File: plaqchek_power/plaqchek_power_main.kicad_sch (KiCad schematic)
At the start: 28 parts, among them U10 LM34601, U12 TPS54202DDC, U15 TPS62175DQC

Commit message: finish schematic
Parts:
- removed U10: LM34601, symbol plaqchek_mlb:LM34601
- added R10, R19, R20, R21, R22, R23, R24, R25, R29, R30: 0R, symbol Device:R_Small_US
- added TP1, TP2, TP3, TP4, TP5, TP6: TestPoint, symbol Connector:TestPoint
- added U2: LM34601, symbol plaqchek:LM34601
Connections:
- net +12V: now also R20.2, R21.2, R22.2; no longer C19.1, C23.1, C24.1, C25.1, C32.1, C39.2, U12.3 (VIN), U15.2 (VIN), U15.3 (EN)
- net +3V3: now also R25.1, TP6.1; no longer C34.1, C35.1, L2.2, R22.1
- net +6V: now also R19.2, R24.1, TP2.1; no longer C40.2, L3.2, R26.1, U15.10 (VOS), U15.8 (~{SLEEP})
- net -6V5: now also R23.1, TP4.1; no longer C23.2, C24.2, C25.2, C27.1, C29.2, C30.2, R24.1
- net GND: now also U2.5 (BIAS)
- net at R23.1, R24.2: now also U2.9 (FB)
- net at U12.5 (EN): now also R10.1
- net at C28.1: now also U2.3 (CBOOT)
- net at C28.2, L1.1: now also U2.1 (SW), U2.2 (SW)
- net at R21.2: now also U2.8 (PGOOD)
- net at C27.2: now also U2.4 (VCC)
- new net: C23.1, C24.1, C25.1, R20.1, R29.2, U2.13 (VIN), U2.14 (VIN)
- new net: C23.2, C24.2, C25.2, C27.1, C29.2, C30.2, R23.2, R24.1, TP3.1, U2.10 (AGND), U2.15 (PGND), U2.16 (PGND)
- new net: C34.1, C35.1, L2.2, R22.1, R25.2, TP5.1
- new net: C19.1, C32.1, R22.1, U12.3 (VIN)
- new net: R19.1, U15.8 (~{SLEEP})
- new net: C39.2, R21.1, R30.1, U15.2 (VIN)
- new net: C40.2, L3.2, R24.2, R26.1, TP1.1, U15.10 (VOS)
- new net: R29.1, U2.12 (EN)
- new net: R30.2, U15.3 (EN)
- no-connect marks 4 -> 5
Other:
- moved on the sheet: C19, C23, C24, C25, C27, C28, C29, C30, C32, C33, C34, C35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

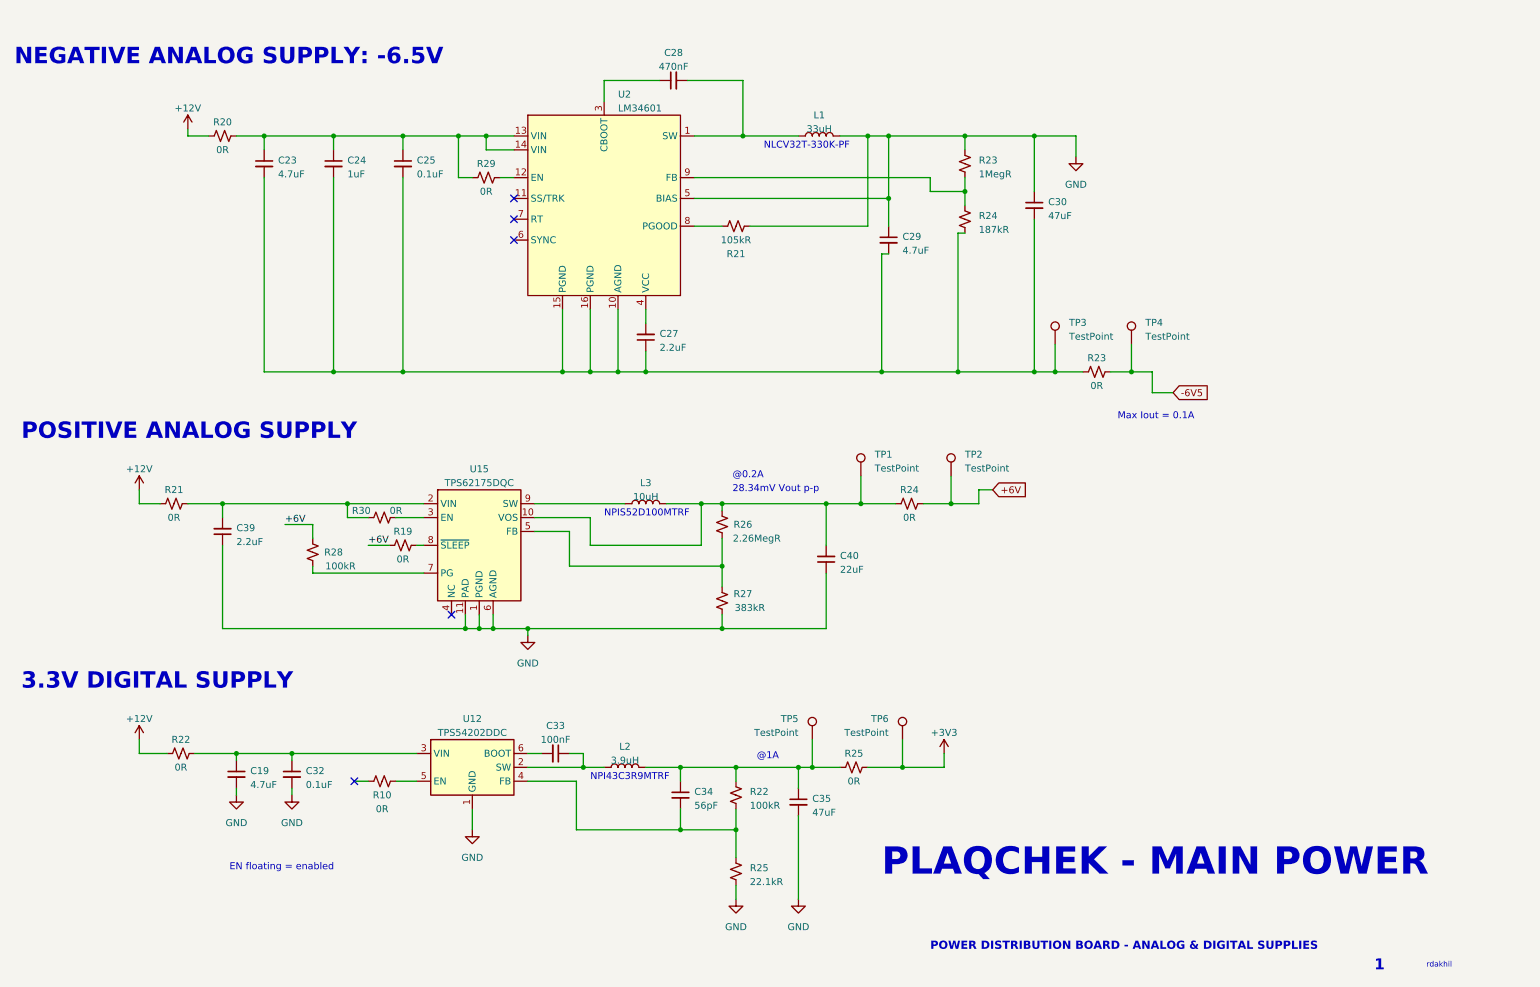
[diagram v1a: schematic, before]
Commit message: more footprints and some value fixes
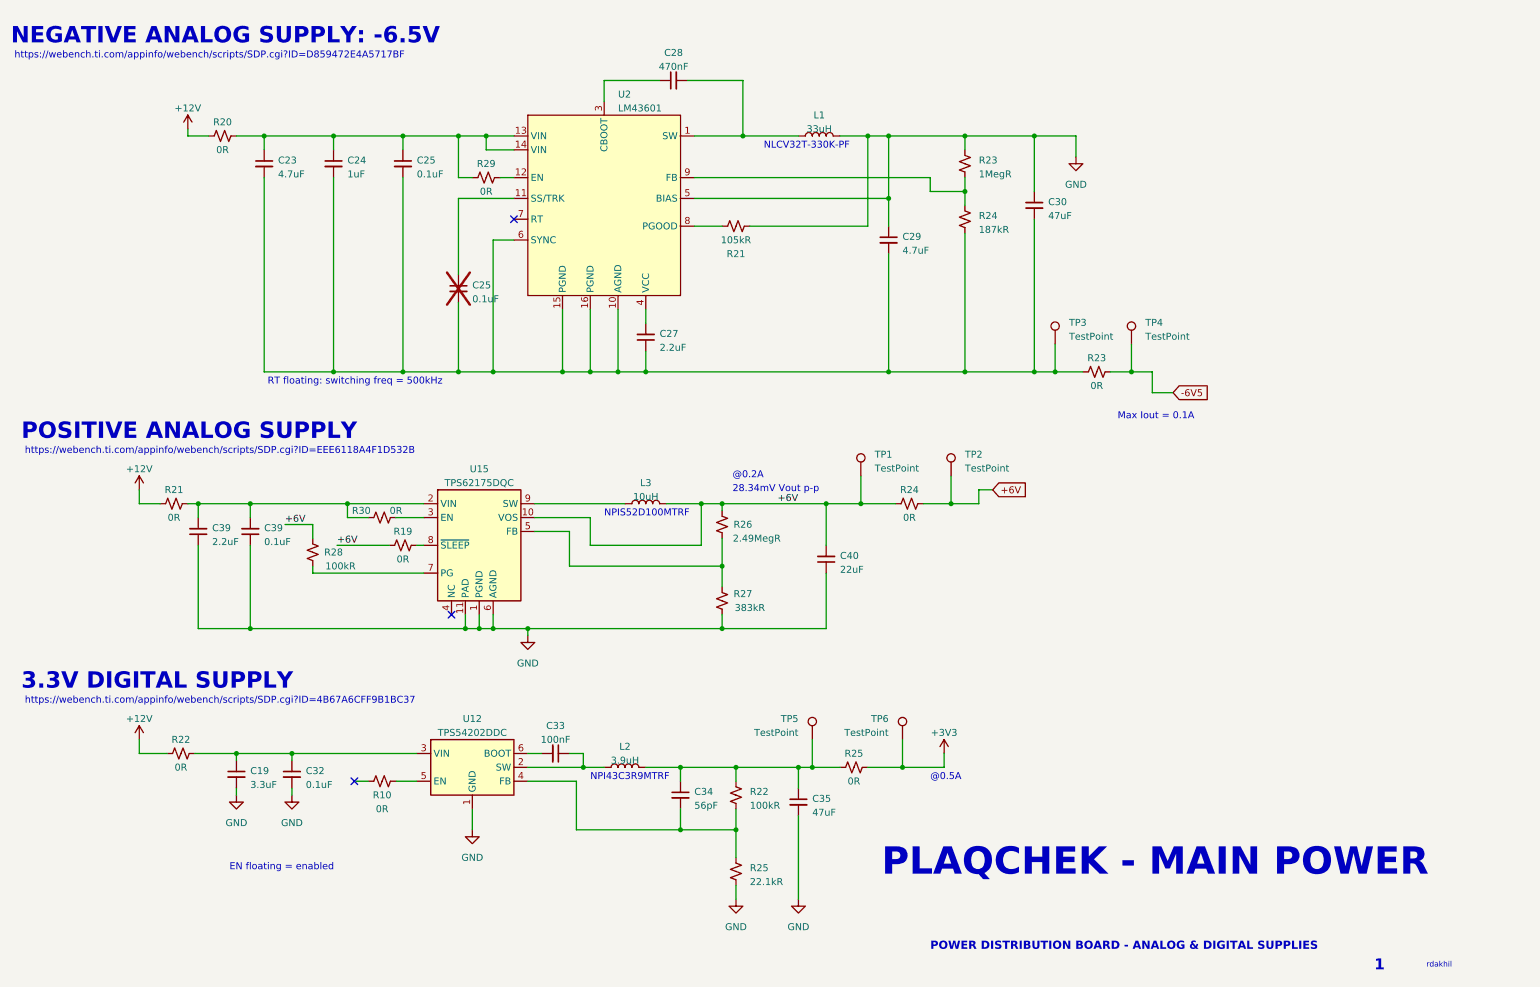
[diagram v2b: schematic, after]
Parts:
- added C25, C39: 0.1uF, Capacitor_SMD:C_0603_1608Metric_Pad1.08x0.95mm_HandSolder, symbol Device:C_Small
- C19: value 4.7uF -> 3.3uF; footprint (none) -> Capacitor_SMD:C_0603_1608Metric_Pad1.08x0.95mm_HandSolder
- C23, C29, C40: footprint (none) -> Capacitor_SMD:C_0805_2012Metric_Pad1.18x1.45mm_HandSolder
- C24, C25, C27, C28, C32, C33, C34, C39: footprint (none) -> Capacitor_SMD:C_0603_1608Metric_Pad1.08x0.95mm_HandSolder
- C30, C35: footprint (none) -> Capacitor_SMD:C_1206_3216Metric_Pad1.33x1.80mm_HandSolder
- R26: value 2.26MegR -> 2.49MegR
- U2: value LM34601 -> LM43601
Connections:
- net +6V: now also C40.2, L3.2, R24.2, R26.1, TP1.1, U15.10 (VOS)
- net GND: now also C39.1
- net at C23.2, C24.2, C25.2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: now also U2.6 (SYNC), C25.2
- net at C39.2, R21.1, R30.1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: now also C39.2
- net at U2.11 (SS/TRK): now also C25.1
- no-connect marks 5 -> 3
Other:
- note added: "@0.5A"
- note added: "RT floating: switching freq = 500kHz"
- note added: "https://webench.ti.com/appinfo/webench/scripts/SDP.cgi?ID=4B67A6CFF9B1BC37"
- note added: "https://webench.ti.com/appinfo/webench/scripts/SDP.cgi?ID=D859472E4A5717BF"
- note added: "https://webench.ti.com/appinfo/webench/scripts/SDP.cgi?ID=EEE6118A4F1D532B"
- note removed: "@1A"
- moved on the sheet: C39

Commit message: finish main logic board PCB routing
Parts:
- L1: footprint (none) -> Inductor_SMD:L_1210_3225Metric_Pad1.42x2.65mm_HandSolder
- R10, R19, R20, R21, R22, R23, R24, R25, R26, R27, R28, R29, R30: footprint (none) -> Resistor_SMD:R_0603_1608Metric_Pad0.98x0.95mm_HandSolder
- U2: footprint (none) -> Package_SO:HTSSOP-16-1EP_4.4x5mm_P0.65mm_EP3.4x5mm
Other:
- note added: "744025100"
- note added: "78438336100"
- note added: "LM43601PWPR"
- note removed: "NPI43C3R9MTRF"
- note removed: "NPIS52D100MTRF"
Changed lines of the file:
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@@
     (effects (font (size 1 1)) (justify left bottom))
+  )
+  (text "LM43601PWPR" (at 109.22 35.56 0)
+    (effects (font (size 1.27 1.27)) (justify left bottom))
   )
   (text "NLCV32T-330K-PF" (at 156.21 43.18 0)
     (effects (font (size 1.27 1.27)) (justify left bottom))
   )
-  (text "NPI43C3R9MTRF\n" (at 124.46 158.75 0)
+  (text "744025100\n" (at 124.46 158.75 0)
     (effects (font (size 1.27 1.27)) (justify left bottom))
   )
@@
     (effects (font (size 1.27 1.27)) (justify left bottom))
   )
-  (text "NPIS52D100MTRF" (at 127 110.49 0)
+  (text "78438336100\n" (at 127 110.49 0)
     (effects (font (size 1.27 1.27)) (justify left bottom))
   )
@@
       (effects (font (size 1.27 1.27)))
     )
-    (property "Footprint" "" (at 57.15 40.64 0)
+    (property "Footprint" "Resistor_SMD:R_0603_1608Metric_Pad0.98x0.95mm_HandSolder" (at 57.15 40.64 0)
       (effects (font (size 1.27 1.27)) hide)
     )
@@
       (effects (font (size 1.27 1.27)) (justify left))
     )
-    (property "Footprint" "" (at 151.13 161.29 0)
+    (property "Footprint" "Resistor_SMD:R_0603_1608Metric_Pad0.98x0.95mm_HandSolder" (at 151.13 161.29 0)
       (effects (font (size 1.27 1.27)) hide)
     )
@@
       (effects (font (size 1.27 1.27)) (justify right))
     )
-    (property "Footprint" "" (at 193.04 45.72 0)
+    (property "Footprint" "Resistor_SMD:R_0603_1608Metric_Pad0.98x0.95mm_HandSolder" (at 193.04 45.72 0)
       (effects (font (size 1.27 1.27)) hide)
     )
@@
       (effects (font (size 1.27 1.27)))
     )
-    (property "Footprint" "" (at 90.17 115.57 0)
+    (property "Footprint" "Resistor_SMD:R_0603_1608Metric_Pad0.98x0.95mm_HandSolder" (at 90.17 115.57 0)
       (effects (font (size 1.27 1.27)) hide)
     )
@@
       (effects (font (size 1.27 1.27)))
     )
-    (property "Footprint" "" (at 48.26 107.95 0)
+    (property "Footprint" "Resistor_SMD:R_0603_1608Metric_Pad0.98x0.95mm_HandSolder" (at 48.26 107.95 0)
       (effects (font (size 1.27 1.27)) hide)
     )
@@
       (effects (font (size 1.27 1.27)))
     )
-    (property "Footprint" "" (at 151.13 57.15 0)
+    (property "Footprint" "Resistor_SMD:R_0603_1608Metric_Pad0.98x0.95mm_HandSolder" (at 151.13 57.15 0)
       (effects (font (size 1.27 1.27)) hide)
     )
@@
       (effects (font (size 1.27 1.27)) (justify left))
     )
-    (property "Footprint" "" (at 138.43 25.4 0)
+    (property "Footprint" "Package_SO:HTSSOP-16-1EP_4.4x5mm_P0.65mm_EP3.4x5mm" (at 138.43 25.4 0)
       (effects (font (size 1.27 1.27)) hide)
     )
@@
       (effects (font (size 1.27 1.27)) (justify left))
     )
-    (property "Footprint" "" (at 151.13 175.26 0)
+    (property "Footprint" "Resistor_SMD:R_0603_1608Metric_Pad0.98x0.95mm_HandSolder" (at 151.13 175.26 0)
       (effects (font (size 1.27 1.27)) hide)
     )
@@
       (effects (font (size 1.27 1.27)))
     )
-    (property "Footprint" "" (at 172.72 156.21 0)
+    (property "Footprint" "Resistor_SMD:R_0603_1608Metric_Pad0.98x0.95mm_HandSolder" (at 172.72 156.21 0)
       (effects (font (size 1.27 1.27)) hide)
     )
@@
       (effects (font (size 1.27 1.27)))
     )
-    (property "Footprint" "" (at 182.88 107.95 0)
+    (property "Footprint" "Resistor_SMD:R_0603_1608Metric_Pad0.98x0.95mm_HandSolder" (at 182.88 107.95 0)
       (effects (font (size 1.27 1.27)) hide)
     )
@@
       (effects (font (size 1.27 1.27)))
     )
-    (property "Footprint" "" (at 148.59 125.73 0)
+    (property "Footprint" "Resistor_SMD:R_0603_1608Metric_Pad0.98x0.95mm_HandSolder" (at 148.59 125.73 0)
       (effects (font (size 1.27 1.27)) hide)
     )
@@
       (effects (font (size 1.27 1.27)))
     )
-    (property "Footprint" "" (at 49.53 153.67 0)
+    (property "Footprint" "Resistor_SMD:R_0603_1608Metric_Pad0.98x0.95mm_HandSolder" (at 49.53 153.67 0)
       (effects (font (size 1.27 1.27)) hide)
     )
@@
       (effects (font (size 1.27 1.27)))
     )
-    (property "Footprint" "" (at 105.41 48.26 0)
+    (property "Footprint" "Resistor_SMD:R_0603_1608Metric_Pad0.98x0.95mm_HandSolder" (at 105.41 48.26 0)
       (effects (font (size 1.27 1.27)) hide)
     )
@@
       (effects (font (size 1.27 1.27)))
     )
-    (property "Footprint" "" (at 86.36 158.75 0)
+    (property "Footprint" "Resistor_SMD:R_0603_1608Metric_Pad0.98x0.95mm_HandSolder" (at 86.36 158.75 0)
       (effects (font (size 1.27 1.27)) hide)
     )
@@
       (effects (font (size 1.27 1.27)))
     )
-    (property "Footprint" "" (at 217.17 83.82 0)
+    (property "Footprint" "Resistor_SMD:R_0603_1608Metric_Pad0.98x0.95mm_HandSolder" (at 217.17 83.82 0)
       (effects (font (size 1.27 1.27)) hide)
     )
@@
       (effects (font (size 1.27 1.27)))
     )
-    (property "Footprint" "" (at 148.59 111.76 0)
+    (property "Footprint" "Resistor_SMD:R_0603_1608Metric_Pad0.98x0.95mm_HandSolder" (at 148.59 111.76 0)
       (effects (font (size 1.27 1.27)) hide)
     )
@@
       (effects (font (size 1.27 1.27)))
     )
-    (property "Footprint" "" (at 73.66 116.84 0)
+    (property "Footprint" "Resistor_SMD:R_0603_1608Metric_Pad0.98x0.95mm_HandSolder" (at 73.66 116.84 0)
       (effects (font (size 1.27 1.27)) hide)
     )
@@
       (effects (font (size 1.27 1.27)) (justify right))
     )
-    (property "Footprint" "" (at 193.04 55.88 0)
+    (property "Footprint" "Resistor_SMD:R_0603_1608Metric_Pad0.98x0.95mm_HandSolder" (at 193.04 55.88 0)
       (effects (font (size 1.27 1.27)) hide)
     )
@@
       (effects (font (size 1.27 1.27)))
     )
-    (property "Footprint" "" (at 86.36 110.49 0)
+    (property "Footprint" "Resistor_SMD:R_0603_1608Metric_Pad0.98x0.95mm_HandSolder" (at 86.36 110.49 0)
       (effects (font (size 1.27 1.27)) hide)
     )
@@
       (effects (font (size 1.27 1.27)))
     )
-    (property "Footprint" "" (at 166.37 40.64 0)
+    (property "Footprint" "Inductor_SMD:L_1210_3225Metric_Pad1.42x2.65mm_HandSolder" (at 166.37 40.64 0)
       (effects (font (size 1.27 1.27)) hide)
     )
@@
       (effects (font (size 1.27 1.27)) hide)
     )
-    (property "Datasheet" "~" (at 130.81 156.21 0)
-      (effects (font (size 1.27 1.27)) hide)
-    )
+    (property "Datasheet" "https://www.we-online.com/components/products/datasheet/744025100.pdf" (at 130.81 156.21 0)
+      (effects (font (size 1.27 1.27)) hide)
+    )

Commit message: finish power board routing, sensing board routing
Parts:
- removed C25: 0.1uF, Capacitor_SMD:C_0603_1608Metric_Pad1.08x0.95mm_HandSolder, symbol Device:C_Small
- removed R29: 0R, Resistor_SMD:R_0603_1608Metric_Pad0.98x0.95mm_HandSolder, symbol Device:R_Small_US
- added C40: 22uF, Capacitor_SMD:C_0805_2012Metric_Pad1.18x1.45mm_HandSolder, symbol Device:C_Small
- L2: value 3.9uH -> 10uH; footprint (none) -> plaqchek:744025100
- L3: footprint (none) -> plaqchek:78438336100
- TP1, TP2, TP3, TP4, TP5, TP6: footprint (none) -> TestPoint:TestPoint_Pad_D1.0mm
- U15: footprint Package_SON:WSON-10-1EP_2x3mm_P0.5mm_EP0.84x2.4mm_ThermalVias -> Package_SON:WSON-10-1EP_2x3mm_P0.5mm_EP0.84x2.4mm
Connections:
- net +6V: no longer C40.2, L3.2, R24.2, R26.1, TP1.1, U15.10 (VOS)
- net GND: now also U15.4 (NC), C40.1
- net VIN_-6V5: now reaches C23.1, C24.1, C25.1, R20.1, U2.13 (VIN), U2.14 (VIN)
- net VIN_-6V5: now also U2.12 (EN)
- net VOUT_-6V5: now reaches C23.2, C24.2, C25.2, C27.1, C29.2, C30.2, R23.2, R24.1, TP3.1, U2.10 (AGND), U2.15 (PGND), U2.16 (PGND), U2.6 (SYNC)
- net VOUT_-6V5: now also U2.17 (PAD)
- net OUT_3V3: now reaches C34.1, C35.1, L2.2, R22.1, R25.2, TP5.1
- net FB_3V3: now reaches C34.2, R22.2, R25.1, U12.4 (FB)
- net FB_-6V5: now reaches R23.1, R24.2, U2.9 (FB)
- net SW_3V3: now reaches C33.1, L2.1, U12.2 (SW)
- net EN_3V3: now reaches R10.1, U12.5 (EN)
- net BOOT_3V3: now reaches C33.2, U12.6 (BOOT)
- net ~{SLP_6V}: now reaches R19.1, U15.8 (~{SLEEP})
- net VIN_6V: now reaches C39.2, C39.2, R21.1, R30.1, U15.2 (VIN)
- net SW_-6V5: now reaches C28.2, L1.1, U2.1 (SW), U2.2 (SW)
- net PG_-6V5: now reaches R21.2, U2.8 (PGOOD)
- net VCC_-6V5: now reaches C27.2, U2.4 (VCC)
- net EN_6V: now reaches R30.2, U15.3 (EN)
- net FB_6V: now reaches R26.2, R27.1, U15.5 (FB)
- net PG_6V: now reaches R28.2, U15.7 (PG)
- net SW_6V: now reaches L3.1, U15.9 (SW)
- new net VOUT_6V: C40.2, C40.2, L3.2, R24.2, R26.1, TP1.1, U15.10 (VOS)
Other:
- note added: "NC recommended to connect to AGND"
- note added: "SS/TRK: floating = internal/default soft-start time capacitor connected to gnd = extended soft-start time"
- note added: "https://webench.ti.com/appinfo/webench/scripts/SDP.cgi?ID=055BFF5AAC301FD0"
- note added: "https://webench.ti.com/appinfo/webench/scripts/SDP.cgi?ID=12BFE4B6BAF5E7F3"
- note removed: "https://webench.ti.com/appinfo/webench/scripts/SDP.cgi?ID=4B67A6CFF9B1BC37"
- note removed: "https://webench.ti.com/appinfo/webench/scripts/SDP.cgi?ID=EEE6118A4F1D532B"
- moved on the sheet: C19, C25, C32, C33, L2, R10, R19, R21, R24, R30, TP1, TP2

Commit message: finish all pcbs, generate gerber files
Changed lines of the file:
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@@
   (junction (at 151.13 167.64) (diameter 0) (color 0 0 0 0)
   )
-  (junction (at 52.705 107.95) (diameter 0) (color 0 0 0 0)
+  (junction (at 52.832 107.95) (diameter 0) (color 0 0 0 0)
   )
   (junction (at 205.74 83.82) (diameter 0) (color 0 0 0 0)
@@
     (stroke (width 0) (type default))
   )
-  (wire (pts (xy 52.705 107.95) (xy 52.705 110.49))
+  (wire (pts (xy 52.832 107.95) (xy 52.832 110.49))
     (stroke (width 0) (type default))
   )
@@
     (stroke (width 0) (type default))
   )
-  (wire (pts (xy 52.705 107.95) (xy 62.23 107.95))
+  (wire (pts (xy 52.832 107.95) (xy 62.23 107.95))
     (stroke (width 0) (type default))
   )
@@
     (stroke (width 0) (type default))
   )
-  (wire (pts (xy 52.705 107.95) (xy 50.8 107.95))
+  (wire (pts (xy 52.832 107.95) (xy 50.8 107.95))
     (stroke (width 0) (type default))
   )
@@
     (stroke (width 0) (type default))
   )
-  (wire (pts (xy 52.705 115.57) (xy 52.705 130.81))
+  (wire (pts (xy 52.832 115.57) (xy 52.832 130.81))
     (stroke (width 0) (type default))
   )
@@
     (stroke (width 0) (type default))
   )
-  (wire (pts (xy 52.705 130.81) (xy 62.23 130.81))
-    (stroke (width 0) (type default))
-  )
-  (wire (pts (xy 78.105 115.57) (xy 82.296 115.57))
+  (wire (pts (xy 52.832 130.81) (xy 62.23 130.81))
+    (stroke (width 0) (type default))
+  )
+  (wire (pts (xy 78.232 115.57) (xy 82.296 115.57))
     (stroke (width 0) (type default))
   )
@@
     (effects (font (size 1.27 1.27)) (justify left bottom))
   )
-  (label "+6V" (at 78.105 115.57 0) (fields_autoplaced)
+  (label "+6V" (at 78.232 115.57 0) (fields_autoplaced)
     (effects (font (size 1.27 1.27)) (justify left bottom))
   )
@@
     )
   )
-  (symbol (lib_id "Device:C_Small") (at 52.705 113.03 180) (unit 1)
-    (in_bom yes) (on_board yes) (dnp no) (fields_autoplaced)
-    (property "Reference" "C39" (at 55.245 112.3886 0)
+  (symbol (lib_id "Device:C_Small") (at 52.832 113.03 180) (unit 1)
+    (in_bom yes) (on_board yes) (dnp no) (fields_autoplaced)
+    (property "Reference" "C39" (at 55.372 112.3886 0)
       (effects (font (size 1.27 1.27)) (justify right))
     )
-    (property "Value" "2.2uF" (at 55.245 114.9286 0)
+    (property "Value" "2.2uF" (at 55.372 114.9286 0)
       (effects (font (size 1.27 1.27)) (justify right))
     )
-    (property "Footprint" "Capacitor_SMD:C_0603_1608Metric_Pad1.08x0.95mm_HandSolder" (at 52.705 113.03 0)
-      (effects (font (size 1.27 1.27)) hide)
-    )
-    (property "Datasheet" "~" (at 52.705 113.03 0)
-      (effects (font (size 1.27 1.27)) hide)
-    )
+    (property "Footprint" "Capacitor_SMD:C_0603_1608Metric_Pad1.08x0.95mm_HandSolder" (at 52.832 113.03 0)
+      (effects (font (size 1.27 1.27)) hide)
+    )
+    (property "Datasheet" "~" (at 52.832 113.03 0)
+      (effects (font (size 1.27 1.27)) hide)
+    )
